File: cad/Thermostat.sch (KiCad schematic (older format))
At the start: 14 parts, among them J1 Screw_Terminal_01x03, J2 Screw_Terminal_01x03, J3 Screw_Terminal_01x02, K1 RSM822, SW1 Rotary_Encoder_Switch, U1 WeMos_mini, U2 ILI9341_LCD_Breakout

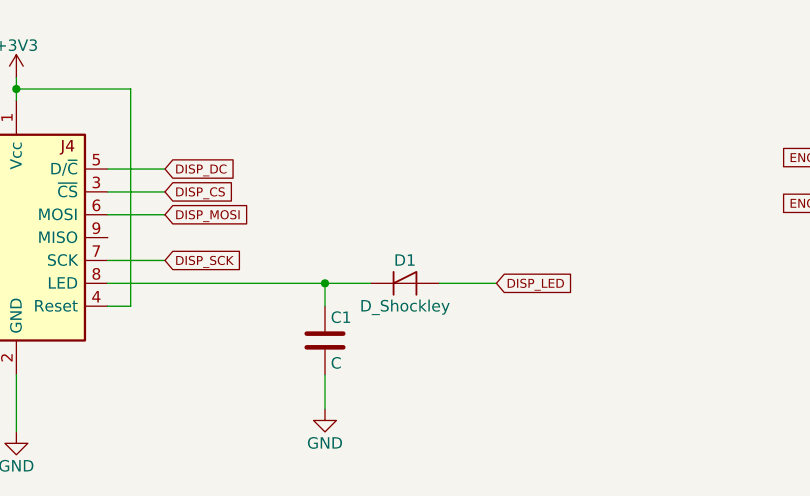
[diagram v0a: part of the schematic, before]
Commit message: Schematic diode correction
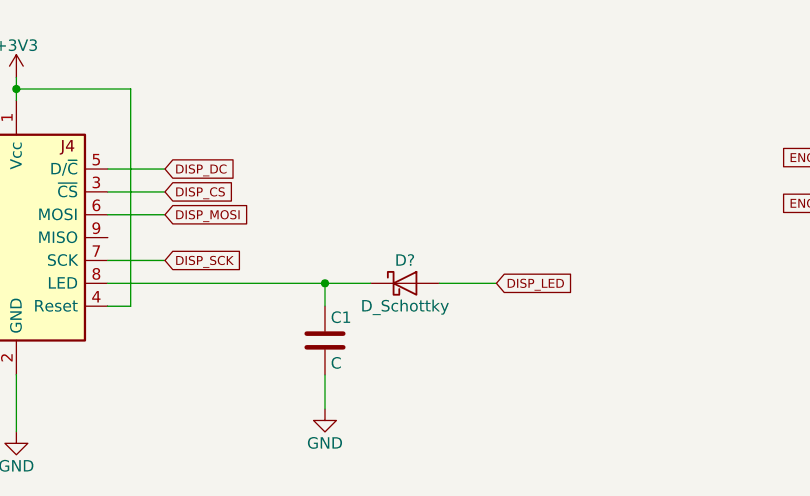
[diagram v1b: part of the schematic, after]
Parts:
- removed D1: D_Shockley, symbol D_Shockley
- added D?: D_Schottky, symbol D_Schottky
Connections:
- net DISP_LED: now also D?.2 (A)
- net at C1.1, U2.8 (LED): now also D?.1 (K)
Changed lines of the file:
@@
 	4600 1550 4450 1550
-$Comp
-L D_Shockley D1
-U 1 1 5BF1A280
-P 4200 3950
-F 0 "D1" H 4200 4050 50  0000 C CNN
-F 1 "D_Shockley" H 4200 3850 50  0000 C CNN
-F 2 "" H 4200 3950 50  0001 C CNN
-F 3 "" H 4200 3950 50  0001 C CNN
-	1    4200 3950
-	1    0    0    -1
-$EndComp
 $Comp
 L RSM822 K1
@@
 Wire Wire Line
 	4500 1050 4500 950
+$Comp
+L D_Schottky D?
+U 1 1 5BF1B09E
+P 4200 3950
+F 0 "D?" H 4200 4050 50  0000 C CNN
+F 1 "D_Schottky" H 4200 3850 50  0000 C CNN
+F 2 "" H 4200 3950 50  0001 C CNN
+F 3 "" H 4200 3950 50  0001 C CNN
+	1    4200 3950
+	1    0    0    -1
+$EndComp
 $EndSCHEMATC

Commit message: PCB
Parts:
- removed J2: Screw_Terminal_01x03, symbol Screw_Terminal_01x03
- removed K1: RSM822, Relays_THT:Relay_DPDT_Finder_40.52, symbol RSM822
- added D4: D, Resistors_Universal:Resistor_SMD+THTuniversal_0805to2512_HandSoldering, symbol D
- added J4: Screw_Terminal_01x02, Connectors_Phoenix:PhoenixContact_MC-GF_02x5.08mm_Angled_ThreadedFlange, symbol Screw_Terminal_01x02
- added RL1: JW2, Relays_THT:Relay_DPDT_Omron_G5V-2, symbol JW2
- added U3: xl-007, xl007:xl007, symbol xl-007
- C1, C2, D2, D3, TH2: footprint (none) -> Resistors_Universal:Resistor_SMD+THTuniversal_0805to2512_HandSoldering
- D1: renamed from D?; footprint (none) -> Resistors_Universal:Resistor_SMD+THTuniversal_0805to2512_HandSoldering
- J1: footprint (none) -> Connectors_Phoenix:PhoenixContact_MC-GF_03x5.08mm_Angled_ThreadedFlange
- J3: footprint (none) -> Connectors_Phoenix:PhoenixContact_MC-GF_02x5.08mm_Angled_ThreadedFlange
- SW1: footprint (none) -> sparkfun:SF-ROTARY-ENCODER
- TH1: footprint (none) -> Sensors:DHT22_Temperature_Humidity
- U1: footprint (none) -> wemos_d1_mini:D1_mini_board
- U2: footprint (none) -> ILI9431:ILI9431 2,8 TFT
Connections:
- net COM1: now also RL1.6
- net GND: now also RL1.8, U3.4 (GND)
- net NC1: now also RL1.7
- net NO1: now also RL1.5
- net RELAY: now also RL1.1
- net pwr: now reaches J3.2 (Pin_2), TH2.2
- net pwr: now also D4.1 (K)
- new net: J4.2 (Pin_2), U3.1 (L)
- new net: J4.1 (Pin_1), U3.2 (N)
- new net: D4.2 (A), U3.3 (+5V)
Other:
- note added: "Power Supply"
- moved on the sheet: C1, C2, D1, D2, D3, J1, J3, SW1, TH1, TH2, U1, U2
